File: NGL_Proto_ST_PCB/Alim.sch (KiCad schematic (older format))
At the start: 15 parts, among them U5 LF33CDT-TR, U6 MAX860ESA+T

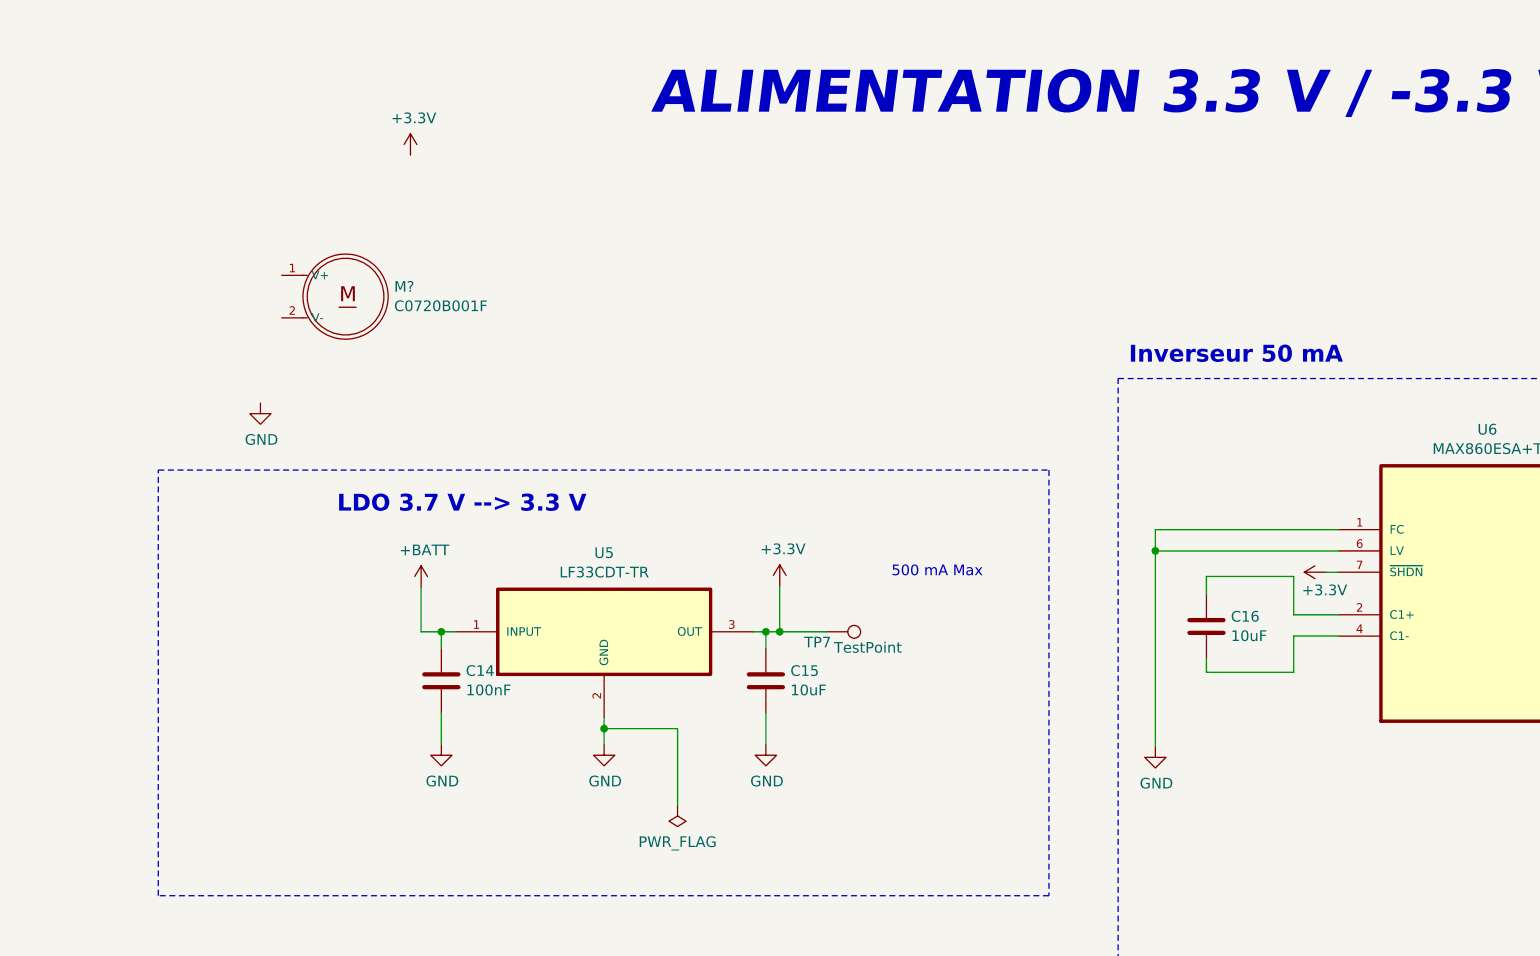
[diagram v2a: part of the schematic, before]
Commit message: Ajuut nouveaux composants: commande 3
Attente question ENABL E + POTAR
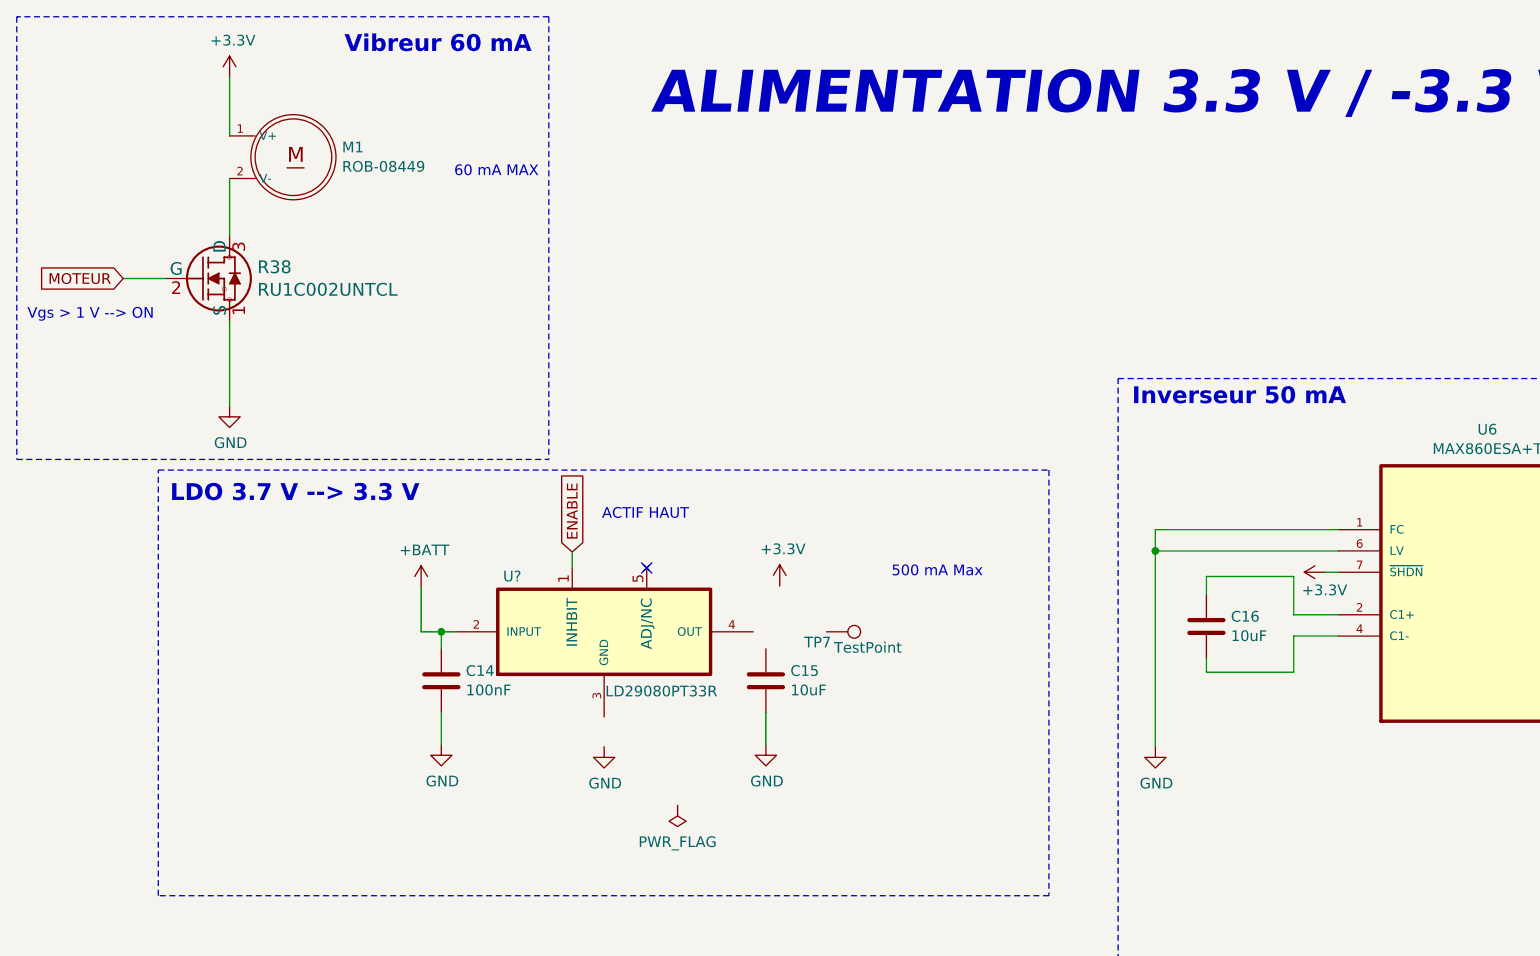
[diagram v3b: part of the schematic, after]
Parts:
- removed U5: LF33CDT-TR, Lib_NGL_Proto:TO228P972X240-3N, symbol LF33CDT-TR:LF33CDT-TR
- added R38: RU1C002UNTCL, Lib_NGL_ST:RU1C002UNTCL, symbol RU1C002UNTCL:RU1C002UNTCL
- added U?: LD29080PT33R, Lib_NGL_ST:DPAK114P990X239-6N, symbol LD29080PT33R:LD29080PT33R
- M1: renamed from M?; value C0720B001F -> ROB-08449; footprint Lib_NGL_ST:XDCR_C0720B001F -> Connector_PinHeader_2.54mm:PinHeader_1x02_P2.54mm_Vertical
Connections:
- net +3V3: now also M1.1 (V+); no longer C15.1, TP7.1
- net +BATT: now also U?.2 (INPUT)
- net -BATT: now also R38.1 (S)
- net at M1.2 (V-): now also R38.3 (D)
- new net ENABLE: U?.1 (INHBIT)
- new net MOTEUR: R38.2 (G)
- no-connect marks 1 -> 2
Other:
- note added: "60 mA MAX"
- note added: "ACTIF HAUT"
- note added: "Vgs > 1 V --> ON"
- note added: "Vibreur 60 mA"
- moved on the sheet: M1
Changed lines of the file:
@@
 	0    1    1    0
 $EndComp
-Text Notes 2005 2910 0    79   ~ 16
+Text Notes 1220 2860 0    79   ~ 16
 LDO 3.7 V --> 3.3 V
 Text Notes 2340 5315 0    79   ~ 16
 Porte pile 18650 + Pont div Sens
-Text Notes 5725 2210 0    79   ~ 16
+Text Notes 5740 2405 0    79   ~ 16
 Inverseur 50 mA
 Wire Wire Line
@@
 $EndComp
 Wire Wire Line
-	4085 3245 4085 3460
-Wire Wire Line
-	3260 3915 3260 3990
-Connection ~ 3260 3915
-Wire Wire Line
-	3605 3915 3260 3915
-Wire Wire Line
-	3605 4275 3605 3915
-Wire Wire Line
 	4020 3840 4020 3990
 $Comp
@@
 Wire Wire Line
 	2495 3990 2495 3840
-Wire Wire Line
-	3260 3860 3260 3915
 $Comp
 L power:GND #PWR026
@@
 	1    0    0    -1
 $EndComp
-Wire Wire Line
-	4020 3460 3960 3460
-Connection ~ 4020 3460
 $Comp
 L Device:C C14
@@
 	1    0    0    -1
 $EndComp
-Wire Wire Line
-	4085 3460 4020 3460
 $Comp
 L power:+3.3V #PWR020
@@
 L power:GND #PWR018
 U 1 1 6271513F
-P 3260 3990
-F 0 "#PWR018" H 3260 3740 50  0001 C CNN
-F 1 "GND" H 3265 3817 50  0000 C CNN
-F 2 "" H 3260 3990 50  0001 C CNN
-F 3 "" H 3260 3990 50  0001 C CNN
-	1    3260 3990
-	1    0    0    -1
-$EndComp
-$Comp
-L LF33CDT-TR:LF33CDT-TR U5
-U 1 1 628ED795
-P 3260 3460
-F 0 "U5" H 3260 3830 50  0000 C CNN
-F 1 "LF33CDT-TR" H 3260 3739 50  0000 C CNN
-F 2 "Lib_NGL_Proto:TO228P972X240-3N" H 3260 3460 50  0001 L BNN
-F 3 "https://www.mouser.fr/datasheet/2/389/cd00000546-1795528.pdf" H 3260 3460 50  0001 L BNN
-F 4 "2253503" H 3260 3460 50  0001 L BNN "OC_FARNELL"
-F 5 "STMicroelectronics" H 3260 3460 50  0001 L BNN "SUPPLIER"
-F 6 "LF33CDT-TR" H 3260 3460 50  0001 L BNN "MPN"
-F 7 "DPAK" H 3260 3460 50  0001 L BNN "PACKAGE"
-F 8 "26M0226" H 3260 3460 50  0001 L BNN "OC_NEWARK"
-	1    3260 3460
+P 3260 4000
+F 0 "#PWR018" H 3260 3750 50  0001 C CNN
+F 1 "GND" H 3265 3827 50  0000 C CNN
+F 2 "" H 3260 4000 50  0001 C CNN
+F 3 "" H 3260 4000 50  0001 C CNN
+	1    3260 4000
 	1    0    0    -1
 $EndComp
@@
 	4135 5545 4135 5705
 Wire Wire Line
-	4020 3460 4020 3540
-Wire Wire Line
-	4305 3460 4085 3460
-Connection ~ 4085 3460
-Wire Wire Line
 	3145 5705 3330 5705
 Wire Wire Line
@@
 	5675 2270 9255 2270
 $Comp
-L C0720B001F:C0720B001F M?
+L C0720B001F:C0720B001F M1
 U 1 1 629D5EFD
-P 2045 1885
-F 0 "M?" H 2273 1931 50  0000 L CNN
-F 1 "C0720B001F" H 2273 1840 50  0000 L CNN
-F 2 "Lib_NGL_ST:XDCR_C0720B001F" H 2045 1885 50  0001 L BNN
-F 3 "" H 2045 1885 50  0001 L BNN
-F 4 "Jinlong Machinery" H 2045 1885 50  0001 L BNN "MF"
-	1    2045 1885
-	1    0    0    -1
-$EndComp
-$Comp
-L power:+3.3V #PWR?
+P 1800 1230
+F 0 "M1" H 2028 1276 50  0000 L CNN
+F 1 "ROB-08449" H 2028 1185 50  0000 L CNN
+F 2 "Connector_PinHeader_2.54mm:PinHeader_1x02_P2.54mm_Vertical" H 1800 1230 50  0001 L BNN
+F 3 "https://www.mouser.fr/datasheet/2/813/B1034_FL45_00_015-2490184.pdf" H 1800 1230 50  0001 L BNN
+F 4 "Jinlong Machinery" H 1800 1230 50  0001 L BNN "MF"
+	1    1800 1230
+	1    0    0    -1
+$EndComp
+$Comp
+L power:+3.3V #PWR047
 U 1 1 629D6C67
-P 2350 1220
-F 0 "#PWR?" H 2350 1070 50  0001 C CNN
-F 1 "+3.3V" H 2365 1393 50  0000 C CNN
-F 2 "" H 2350 1220 50  0001 C CNN
-F 3 "" H 2350 1220 50  0001 C CNN
-	1    2350 1220
-	1    0    0    -1
-$EndComp
-$Comp
-L power:GND #PWR?
+P 1500 855
+F 0 "#PWR047" H 1500 705 50  0001 C CNN
+F 1 "+3.3V" H 1515 1028 50  0000 C CNN
+F 2 "" H 1500 855 50  0001 C CNN
+F 3 "" H 1500 855 50  0001 C CNN
+	1    1500 855
+	1    0    0    -1
+$EndComp
+$Comp
+L power:GND #PWR062
 U 1 1 629D766E
-P 1645 2385
-F 0 "#PWR?" H 1645 2135 50  0001 C CNN
-F 1 "GND" H 1650 2212 50  0000 C CNN
-F 2 "" H 1645 2385 50  0001 C CNN
-F 3 "" H 1645 2385 50  0001 C CNN
-	1    1645 2385
-	1    0    0    -1
-$EndComp
+P 1500 2400
+F 0 "#PWR062" H 1500 2150 50  0001 C CNN
+F 1 "GND" H 1505 2227 50  0000 C CNN
+F 2 "" H 1500 2400 50  0001 C CNN
+F 3 "" H 1500 2400 50  0001 C CNN
+	1    1500 2400
+	1    0    0    -1
+$EndComp
+$Comp
+L RU1C002UNTCL:RU1C002UNTCL R38
+U 1 1 62A199F1
+P 1200 1800
+F 0 "R38" H 1630 1853 60  0000 L CNN
+F 1 "RU1C002UNTCL" H 1630 1747 60  0000 L CNN
+F 2 "Lib_NGL_ST:RU1C002UNTCL" H 1650 1540 60  0001 C CNN
+F 3 "https://www.mouser.fr/datasheet/2/348/ru1c002untcl-e-1873370.pdf" H 1630 1694 60  0001 L CNN
+	1    1200 1800
+	1    0    0    -1
+$EndComp
+Text Notes 2555 1330 0    50   ~ 0
+60 mA MAX
+Text GLabel 1000 1800 0    50   Input ~ 0
+MOTEUR
+Wire Wire Line
+	1500 2400 1500 2000
+Wire Wire Line
+	1200 1800 1000 1800
+Wire Wire Line
+	1500 1600 1500 1330
+Wire Wire Line
+	1500 1130 1500 855
+Text Notes 550  2000 0    50   ~ 0
+Vgs > 1 V --> ON
+Wire Notes Line
+	3000 570  500  570
+Wire Notes Line
+	500  570  500  2650
+Wire Notes Line
+	500  2650 3000 2650
+Wire Notes Line
+	3000 570  3000 2650
+Text Notes 2040 750  0    79   ~ 16
+Vibreur 60 mA
+$Comp
+L LD29080PT33R:LD29080PT33R U?
+U 1 1 62A532E3
+P 3260 3460
+F 0 "U?" H 2785 3720 50  0000 L CNN
+F 1 "LD29080PT33R" H 3265 3180 50  0000 L CNN
+F 2 "Lib_NGL_ST:DPAK114P990X239-6N" H 3260 3460 50  0001 L BNN
+F 3 "https://www.mouser.fr/datasheet/2/389/cd00044919-1796076.pdf" H 3260 3460 50  0001 L BNN
+F 4 "2253503" H 3260 3460 50  0001 L BNN "OC_FARNELL"
+F 5 "STMicroelectronics" H 3260 3460 50  0001 L BNN "SUPPLIER"
+F 6 "LF33CDT-TR" H 3260 3460 50  0001 L BNN "MPN"
+F 7 "DPAK" H 3260 3460 50  0001 L BNN "PACKAGE"
+F 8 "26M0226" H 3260 3460 50  0001 L BNN "OC_NEWARK"
+	1    3260 3460
+	1    0    0    -1
+$EndComp
+NoConn ~ 3460 3160
+Text GLabel 3110 3085 1    50   Input ~ 0
+ENABLE
+Text Notes 3250 2940 0    50   ~ 0
+ACTIF HAUT
+Wire Wire Line
+	3110 3160 3110 3085
 $EndSCHEMATC

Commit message: Avancement après réunion mercredi
finir pour mettre en review puis attente.
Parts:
- removed U6: MAX860ESA+T, Lib_NGL_Proto:SOIC127P600X175-8N, symbol MAX860ESA_T:MAX860ESA+T
- added U?: MAX1680ESA+T, Lib_NGL_ST:SOIC127P600X175-8N, symbol MAX1680ESA_T:MAX1680ESA+T
- C16: value 10uF -> 4.7uF
- gave numbers to parts that had none: 1
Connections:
- net +3V3: now also C15.1, TP7.1, U5.4 (OUT), U?.8 (IN)
- net -3V3: now also U?.5 (OUT)
- net -BATT: now also U5.3 (GND), U?.1 (FSEL), U?.3 (GND), U?.6 (LV), U?.7 (SHDN)
- net at C16.1: now also U?.2 (CAP+)
- net at C16.2: now also U?.4 (CAP-)
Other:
- note added: "Inverseur 125 mA (avant 50 mA)"
- note added: "Switching frequency:\n250 kHz --> Fsel = LV\n125 kHz --> Fsel = IN"
- note removed: "Inverseur 50 mA"
- moved on the sheet: C17, TP8

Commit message: Commit avant DSN
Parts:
- C14, C15, C16, C17: footprint Capacitor_SMD:C_0805_2012Metric -> Capacitor_SMD:C_0805_2012Metric_Pad1.18x1.45mm_HandSolder
- R1, R5: footprint Resistor_SMD:R_0805_2012Metric -> Resistor_SMD:R_0805_2012Metric_Pad1.20x1.40mm_HandSolder
- gave numbers to parts that had none: 1
- renumbered R38 to T1
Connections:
- net +3V3: now also U6.1 (FSEL)
- net +BATT: now also BT1.P, TPP2.1; no longer S1.1
- net -BATT: no longer U6.1 (FSEL)
- net OUT_BAT: now also S1.1
- net ENABLE renamed INH
- net INH: now also S1.2
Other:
- note added: "800 mA Max"
- note added: "ACTIF HAUT > 2V"
- note added: "Switching frequency:\n250 kHz --> Fsel = LV\n*125 kHz --> Fsel = IN"
- note removed: "500 mA Max"
- note removed: "ACTIF HAUT"
- note removed: "Switching frequency:\n250 kHz --> Fsel = LV\n125 kHz --> Fsel = IN"
- moved on the sheet: S1
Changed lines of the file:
@@
 encoding utf-8
 Sheet 3 6
-Title "NGL_Proto_V2"
-Date "2022-05-27"
-Rev "V2"
+Title "NGL_Proto_ST"
+Date "2022-06-09"
+Rev "V1.1"
 Comp "ADTP"
 Comment1 "Auteur: Benoît"
@@
 F 0 "C16" H 6205 3481 50  0000 L CNN
 F 1 "4.7uF" H 6205 3390 50  0000 L CNN
-F 2 "Capacitor_SMD:C_0805_2012Metric" H 6128 3285 50  0001 C CNN
+F 2 "Capacitor_SMD:C_0805_2012Metric_Pad1.18x1.45mm_HandSolder" H 6128 3285 50  0001 C CNN
 F 3 "~" H 6090 3435 50  0001 C CNN
 	1    6090 3435
@@
 F 0 "C17" H 8255 3081 50  0000 L CNN
 F 1 "10uF" H 8255 2990 50  0000 L CNN
-F 2 "Capacitor_SMD:C_0805_2012Metric" H 8178 2885 50  0001 C CNN
+F 2 "Capacitor_SMD:C_0805_2012Metric_Pad1.18x1.45mm_HandSolder" H 8178 2885 50  0001 C CNN
 F 3 "~" H 8140 3035 50  0001 C CNN
 	1    8140 3035
@@
 Wire Wire Line
 	6710 2980 5850 2980
-Wire Wire Line
-	5850 2980 5850 3080
-Connection ~ 5850 3080
 $Comp
 L Connector:TestPoint TP8
@@
 	0    1    1    0
 $EndComp
-Text Notes 1220 2860 0    79   ~ 16
+Text Notes 3880 2880 0    79   ~ 16
 LDO 3.7 V --> 3.3 V
 Text Notes 2340 5315 0    79   ~ 16
 Porte pile 18650 + Pont div Sens
-Text Notes 5740 2405 0    79   ~ 16
+Text Notes 6325 2390 0    79   ~ 16
 Inverseur 125 mA (avant 50 mA)
 Wire Wire Line
@@
 F 0 "R1" H 2200 6081 50  0000 L CNN
 F 1 "300K" H 2200 5990 50  0000 L CNN
-F 2 "Resistor_SMD:R_0805_2012Metric" V 2060 6035 50  0001 C CNN
+F 2 "Resistor_SMD:R_0805_2012Metric_Pad1.20x1.40mm_HandSolder" V 2060 6035 50  0001 C CNN
 F 3 "~" H 2130 6035 50  0001 C CNN
 	1    2130 6035
@@
 F 0 "R5" H 2200 6496 50  0000 L CNN
 F 1 "1M" H 2200 6405 50  0000 L CNN
-F 2 "Resistor_SMD:R_0805_2012Metric" V 2060 6450 50  0001 C CNN
+F 2 "Resistor_SMD:R_0805_2012Metric_Pad1.20x1.40mm_HandSolder" V 2060 6450 50  0001 C CNN
 F 3 "~" H 2130 6450 50  0001 C CNN
 	1    2130 6450
@@
 F 0 "C14" H 2610 3736 50  0000 L CNN
 F 1 "100nF" H 2610 3645 50  0000 L CNN
-F 2 "Capacitor_SMD:C_0805_2012Metric" H 2533 3540 50  0001 C CNN
+F 2 "Capacitor_SMD:C_0805_2012Metric_Pad1.18x1.45mm_HandSolder" H 2533 3540 50  0001 C CNN
 F 3 "~" H 2495 3690 50  0001 C CNN
 	1    2495 3690
@@
 F 0 "C15" H 4135 3736 50  0000 L CNN
 F 1 "10uF" H 4135 3645 50  0000 L CNN
-F 2 "Capacitor_SMD:C_0805_2012Metric" H 4058 3540 50  0001 C CNN
+F 2 "Capacitor_SMD:C_0805_2012Metric_Pad1.18x1.45mm_HandSolder" H 4058 3540 50  0001 C CNN
 F 3 "~" H 4020 3690 50  0001 C CNN
 	1    4020 3690
@@
 	1165 4700 1165 2700
 Text Notes 4610 3210 0    50   ~ 0
-500 mA Max
+800 mA Max
 $Comp
 L 1101M2S3CQE2:1101M2S3CQE2 S1
 U 1 1 62A4F233
-P 3045 5705
-F 0 "S1" H 3095 5927 50  0000 C CNN
-F 1 "1101M2S3CQE2" H 3095 5928 50  0001 C CNN
-F 2 "Lib_NGL_Proto:SW_1101M2S3CQE2" H 3045 5705 50  0001 L BNN
-F 3 "https://docs.rs-online.com/eaa8/0900766b800993da.pdf" H 3045 5705 50  0001 L BNN
-F 4 "CnK" H 3045 5705 50  0001 L BNN "MANUFACTURER"
-	1    3045 5705
+P 1895 2910
+F 0 "S1" H 1945 3132 50  0000 C CNN
+F 1 "1101M2S3CQE2" H 1945 3133 50  0001 C CNN
+F 2 "Lib_NGL_Proto:SW_1101M2S3CQE2" H 1895 2910 50  0001 L BNN
+F 3 "https://docs.rs-online.com/eaa8/0900766b800993da.pdf" H 1895 2910 50  0001 L BNN
+F 4 "CnK" H 1895 2910 50  0001 L BNN "MANUFACTURER"
+	1    1895 2910
 	-1   0    0    1
 $EndComp
@@
 Wire Wire Line
 	4135 5545 4135 5705
-Wire Wire Line
-	3145 5705 3330 5705
-Wire Wire Line
-	2130 5885 2130 5805
-Wire Wire Line
-	2845 5805 2130 5805
-Connection ~ 2130 5805
-Wire Wire Line
-	2130 5805 2130 5610
 Wire Wire Line
 	1780 5510 1780 5610
@@
 	2400 3460 2400 3250
 Connection ~ 2495 3460
-NoConn ~ 2845 5605
 Text Label 8295 2680 0    50   ~ 0
 +3V3
@@
 $EndComp
 $Comp
-L RU1C002UNTCL:RU1C002UNTCL R38
+L RU1C002UNTCL:RU1C002UNTCL T1
 U 1 1 62A199F1
 P 1200 1800
-F 0 "R38" H 1630 1853 60  0000 L CNN
+F 0 "T1" H 1630 1853 60  0000 L CNN
 F 1 "RU1C002UNTCL" H 1630 1747 60  0000 L CNN
 F 2 "Lib_NGL_ST:RU1C002UNTCL" H 1650 1540 60  0001 C CNN
@@
 $EndComp
 NoConn ~ 3460 3160
-Text GLabel 3110 3085 1    50   Input ~ 0
-ENABLE
-Text Notes 3250 2940 0    50   ~ 0
-ACTIF HAUT
-Wire Wire Line
-	3110 3160 3110 3085
+Text Notes 2490 2835 0    50   ~ 0
+ACTIF HAUT > 2V
 Wire Wire Line
 	3260 4000 3260 3915
@@
 	2540 6240 2130 6240
 $Comp
-L MAX1680ESA_T:MAX1680ESA+T U?
+L MAX1680ESA_T:MAX1680ESA+T U6
 U 1 1 62BE87B3
 P 7310 3180
-F 0 "U?" H 7310 3947 50  0000 C CNN
+F 0 "U6" H 7310 3947 50  0000 C CNN
 F 1 "MAX1680ESA+T" H 7310 3856 50  0000 C CNN
 F 2 "Lib_NGL_ST:SOIC127P600X175-8N" H 7310 3180 50  0001 L BNN
@@
 	5850 3180 5850 3080
 Text Notes 5725 6250 0    50   ~ 0
-Switching frequency:\n250 kHz --> Fsel = LV\n125 kHz --> Fsel = IN
+Switching frequency:\n250 kHz --> Fsel = LV\n*125 kHz --> Fsel = IN
+Wire Wire Line
+	2130 5610 2130 5705
+Text GLabel 1575 3010 0    50   Input ~ 0
+REG_EN
+Wire Wire Line
+	1575 3010 1695 3010
+Wire Wire Line
+	1995 2910 3110 2910
+Wire Wire Line
+	3110 2910 3110 3160
+NoConn ~ 1695 2810
+Wire Wire Line
+	2130 5705 3330 5705
+Connection ~ 2130 5705
+Wire Wire Line
+	2130 5705 2130 5885
+Text GLabel 3460 2910 2    50   Output ~ 0
+INH
+Wire Wire Line
+	3460 2910 3110 2910
+Connection ~ 3110 2910
+$Comp
+L power:+3.3V #PWR0116
+U 1 1 62AC51E7
+P 5850 2585
+F 0 "#PWR0116" H 5850 2435 50  0001 C CNN
+F 1 "+3.3V" H 5865 2758 50  0000 C CNN
+F 2 "" H 5850 2585 50  0001 C CNN
+F 3 "" H 5850 2585 50  0001 C CNN
+	1    5850 2585
+	1    0    0    -1
+$EndComp
+Wire Wire Line
+	5850 2980 5850 2585
 $EndSCHEMATC
